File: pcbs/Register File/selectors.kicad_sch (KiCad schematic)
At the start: 1 part, among them U1001 74HC138

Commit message: More work
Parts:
- added R401 (x8): 220k, Resistor_SMD:R_0603_1608Metric, symbol Device:R
- added U1002, U1003, U1004: 74HC138, Package_DIP:DIP-16_W7.62mm_Socket, symbol 74xx:74HC138
- added U1005: 74HC540, Package_DIP:DIP-20_W7.62mm_Socket, symbol 74xx:74LS540
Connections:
- net +5V: now also U1002.16 (VCC), U1003.16 (VCC), U1004.16 (VCC), U1005.20 (VCC)
- net GND: now also R401.2, R401.2, R401.2, R401.2, R401.2, R401.2, R401.2, R401.2, U1002.8 (GND), U1003.8 (GND), U1004.8 (GND), U1005.10 (GND)
- new net: U1004.15 (~{Y0}), U1005.2 (A0)
- new net: U1004.14 (~{Y1}), U1005.3 (A1)
- new net: U1004.13 (~{Y2}), U1005.4 (A2)
- new net: U1004.12 (~{Y3}), U1005.5 (A3)
- new net: U1004.11 (~{Y4}), U1005.6 (A4)
- new net: U1004.10 (~{Y5}), U1005.7 (A5)
- new net: U1004.9 (~{Y6}), U1005.8 (A6)
- new net: U1004.7 (~{Y7}), U1005.9 (A7)
- new net C_{Write}0: R401.1, U1005.18 (Y0)
- new net C_{Write}1: R401.1, U1005.17 (Y1)
- new net C_{Write}2: R401.1, U1005.16 (Y2)
- new net C_{Write}3: R401.1, U1005.15 (Y3)
- new net C_{Write}4: R401.1, U1005.14 (Y4)
- new net C_{Write}5: R401.1, U1005.13 (Y5)
- new net C_{Write}6: R401.1, U1005.12 (Y6)
- new net C_{Write}7: R401.1, U1005.11 (Y7)
- new net R_{B}0: U1002.1 (A0)
- new net R_{B}1: U1002.2 (A1)
- new net R_{B}2: U1002.3 (A2)
- new net R_{C}0: U1003.1 (A0), U1004.1 (A0)
- new net R_{C}1: U1003.2 (A1), U1004.2 (A1)
- new net R_{C}2: U1003.3 (A2), U1004.3 (A2)
- new net ~{B_{select}}0: U1002.15 (~{Y0})
- new net ~{B_{select}}1: U1002.14 (~{Y1})
- new net ~{B_{select}}2: U1002.13 (~{Y2})
- new net ~{B_{select}}3: U1002.12 (~{Y3})
- new net ~{B_{select}}4: U1002.11 (~{Y4})
- new net ~{B_{select}}5: U1002.10 (~{Y5})
- new net ~{B_{select}}6: U1002.9 (~{Y6})
- new net ~{B_{select}}7: U1002.7 (~{Y7})
- new net ~{C_{select}}0: U1003.15 (~{Y0})
- new net ~{C_{select}}1: U1003.14 (~{Y1})
- new net ~{C_{select}}2: U1003.13 (~{Y2})
- new net ~{C_{select}}3: U1003.12 (~{Y3})
- new net ~{C_{select}}4: U1003.11 (~{Y4})
- new net ~{C_{select}}5: U1003.10 (~{Y5})
- new net ~{C_{select}}6: U1003.9 (~{Y6})
- new net ~{C_{select}}7: U1003.7 (~{Y7})
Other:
- moved on the sheet: U1001

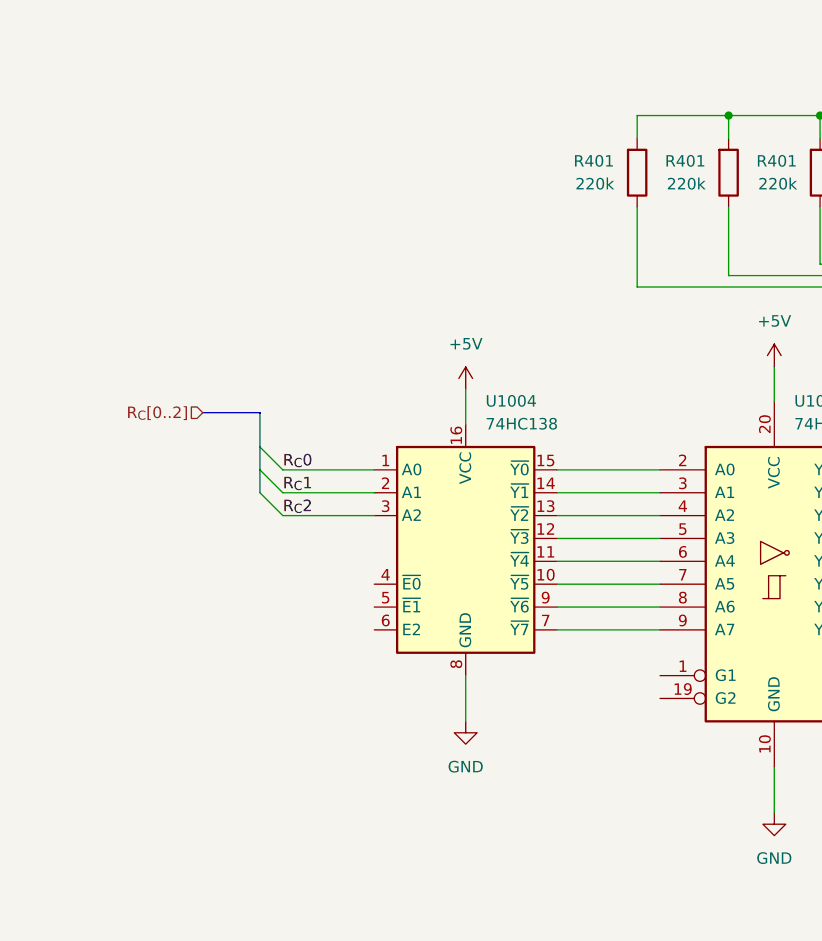
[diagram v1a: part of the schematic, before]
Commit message: Adding some capacitors
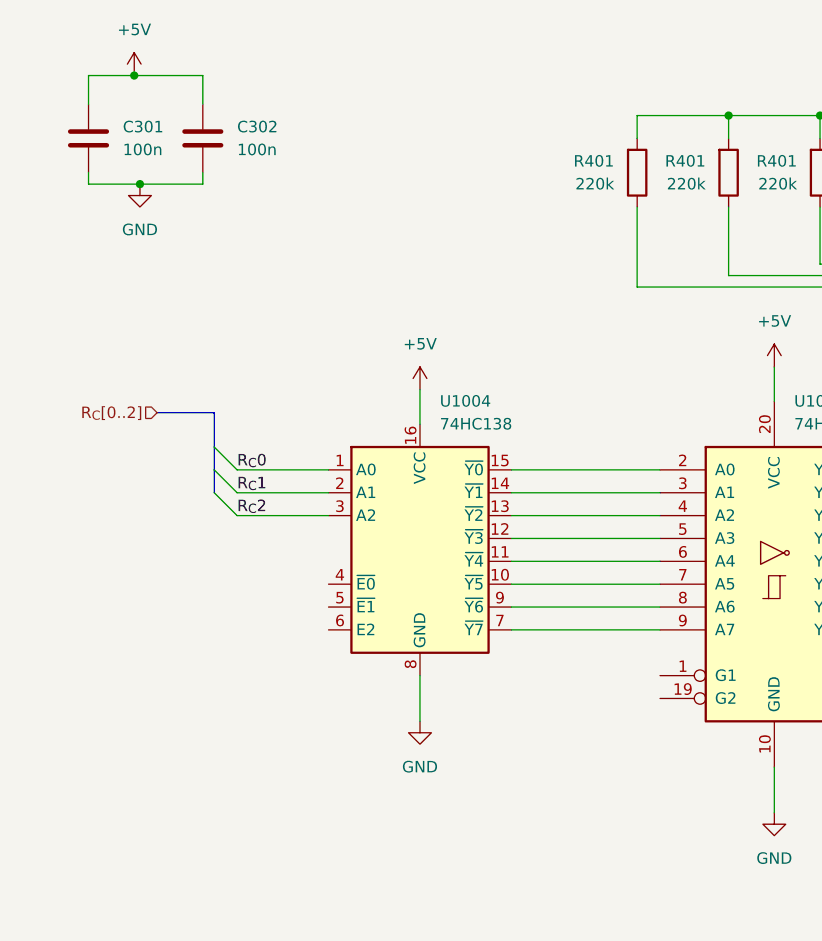
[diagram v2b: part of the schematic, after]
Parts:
- added C301, C302: 100n, Capacitor_SMD:C_0603_1608Metric, symbol Device:C
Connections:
- net +5V: now also C301.1, C302.1
- net GND: now also C301.2, C302.2
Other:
- moved on the sheet: U1004

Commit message: Lots of LEDs
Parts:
- added D801 (x8): YELLOW, LED_SMD:LED_0603_1608Metric, symbol Device:LED
- added R809, R810, R811, R812, R813, R814, R815, R816: 4k7, Resistor_SMD:R_0603_1608Metric, symbol Device:R
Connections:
- net +5V: now also D801.2 (A), D801.2 (A), D801.2 (A), D801.2 (A), D801.2 (A), D801.2 (A), D801.2 (A), D801.2 (A)
- net W0: now reaches U1004.15 (~{Y0}), U1005.2 (A0)
- net W0: now also R809.1
- net W1: now reaches U1004.14 (~{Y1}), U1005.3 (A1)
- net W1: now also R810.1
- net W2: now reaches U1004.13 (~{Y2}), U1005.4 (A2)
- net W2: now also R811.1
- net W3: now reaches U1004.12 (~{Y3}), U1005.5 (A3)
- net W3: now also R812.1
- net W4: now reaches U1004.11 (~{Y4}), U1005.6 (A4)
- net W4: now also R813.1
- net W5: now reaches U1004.10 (~{Y5}), U1005.7 (A5)
- net W5: now also R814.1
- net W6: now reaches U1004.9 (~{Y6}), U1005.8 (A6)
- net W6: now also R815.1
- net W7: now reaches U1004.7 (~{Y7}), U1005.9 (A7)
- net W7: now also R816.1
- new net: D801.1 (K), R815.2
- new net: D801.1 (K), R809.2
- new net: D801.1 (K), R811.2
- new net: D801.1 (K), R816.2
- new net: D801.1 (K), R814.2
- new net: D801.1 (K), R810.2
- new net: D801.1 (K), R813.2
- new net: D801.1 (K), R812.2

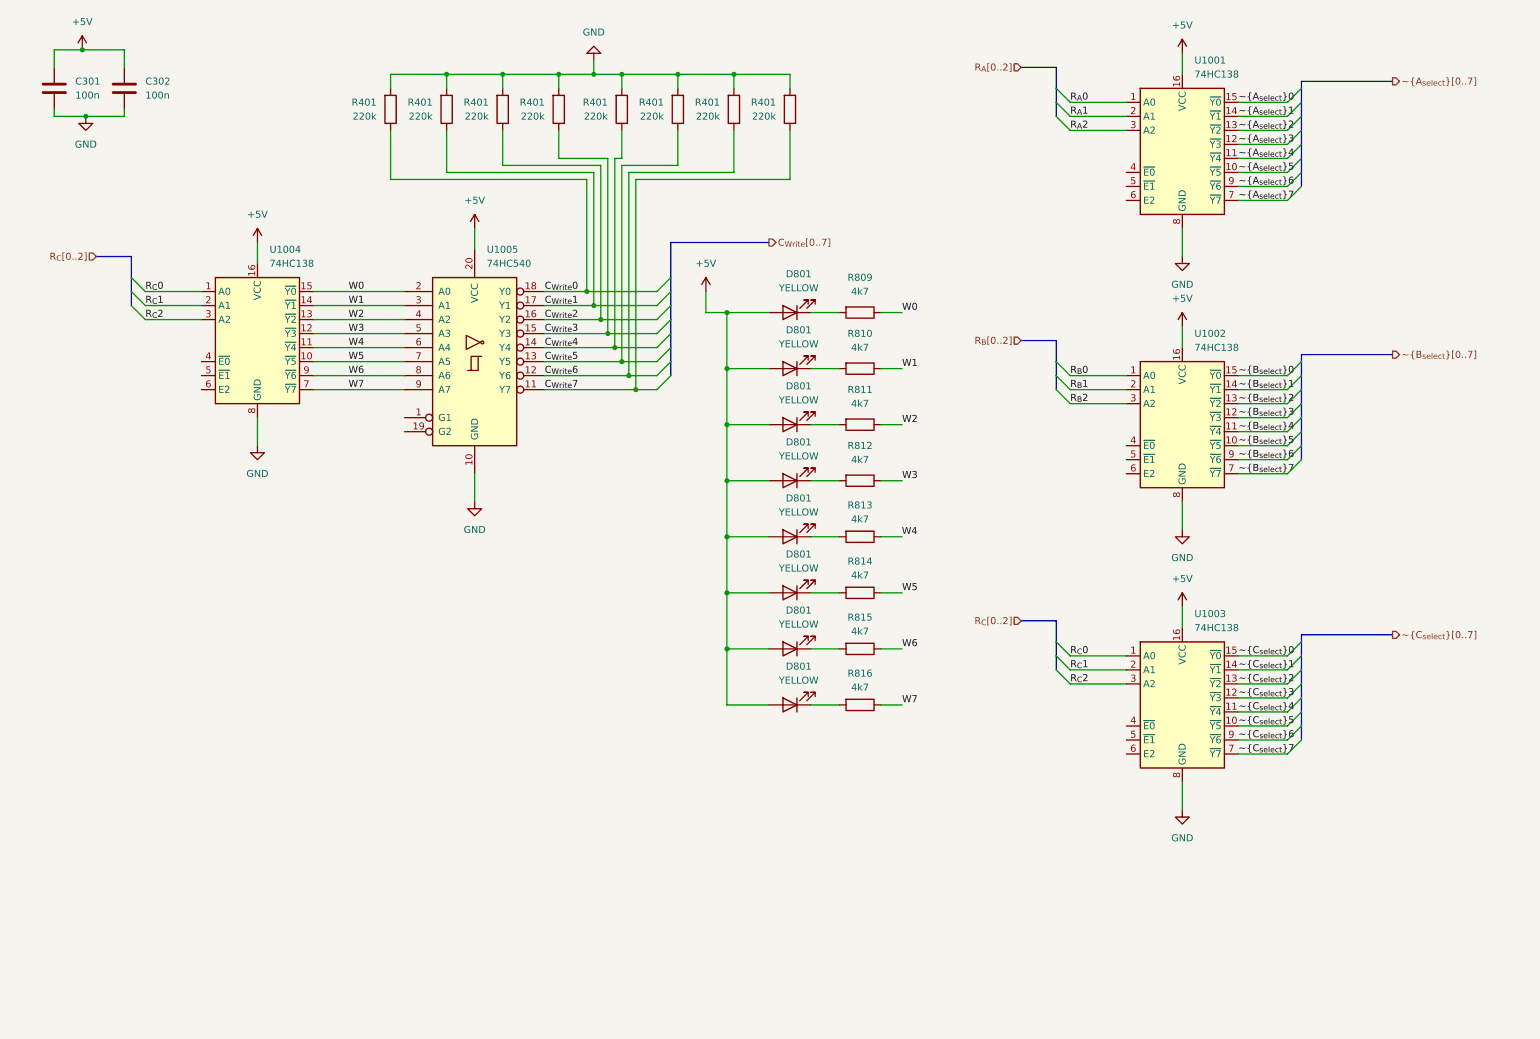
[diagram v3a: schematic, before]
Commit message: More control logic
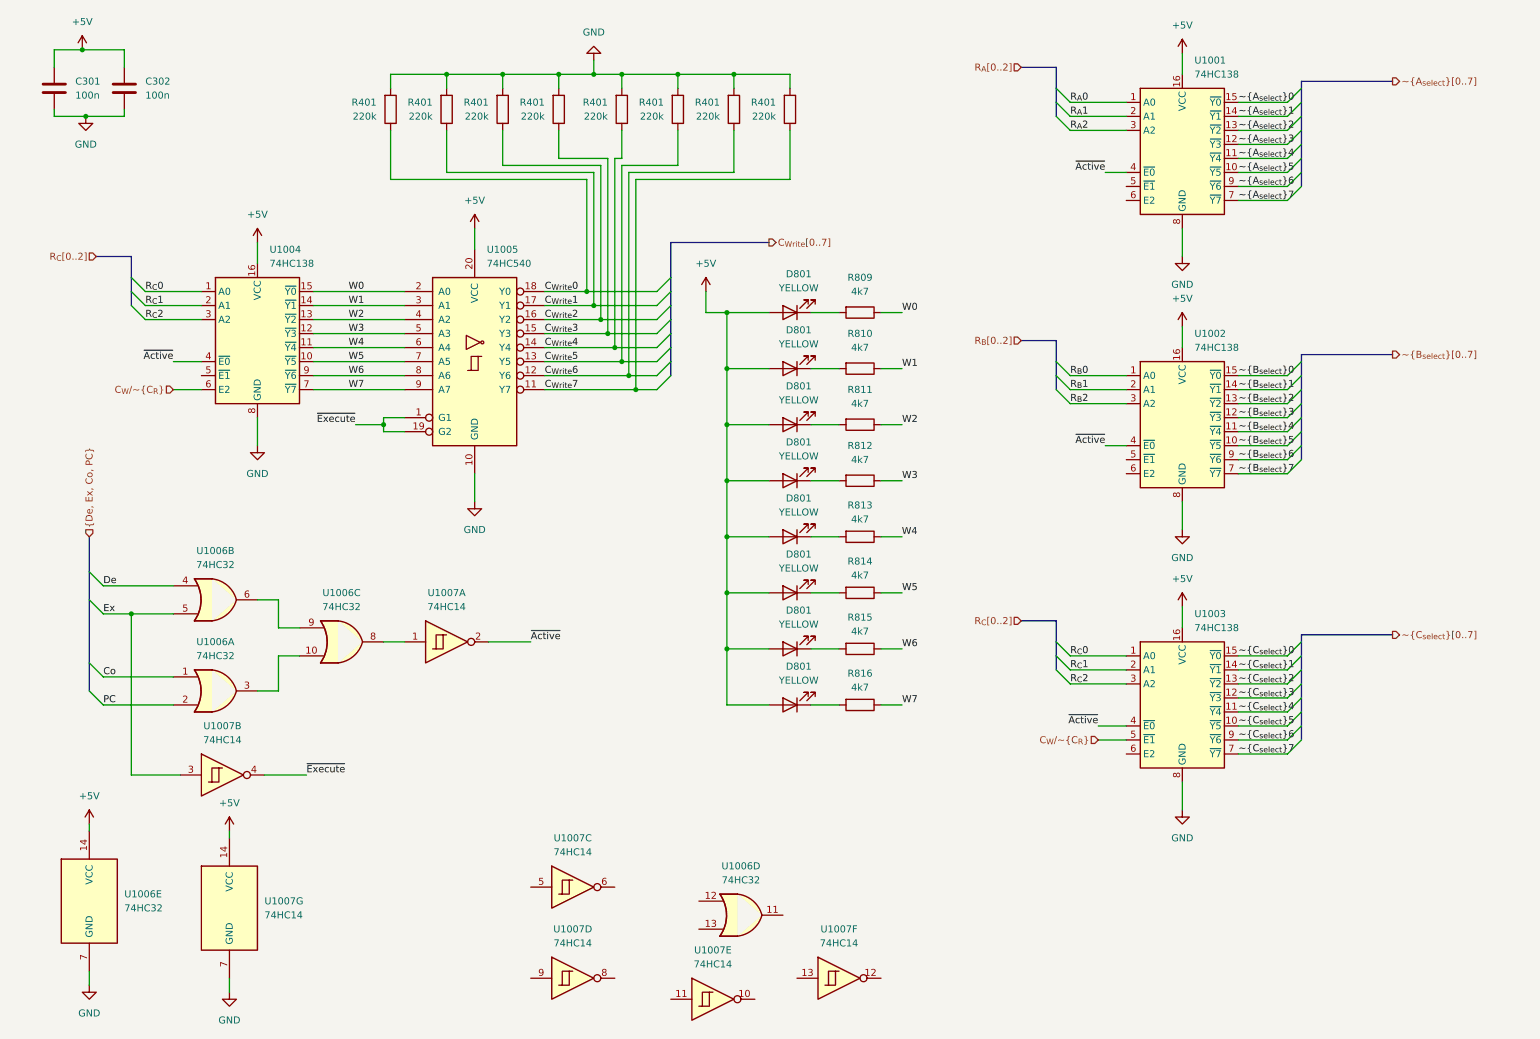
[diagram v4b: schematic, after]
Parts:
- added U1006: 74HC32, Package_DIP:DIP-14_W7.62mm_Socket, symbol 74xx:74LS32
- added U1007: 74HC14, Package_SO:SOIC-14_3.9x8.7mm_P1.27mm, symbol 74xx:74HC14
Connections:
- net +5V: now also U1006.14 (VCC), U1007.14 (VCC)
- net GND: now also U1006.7 (GND), U1007.7 (GND)
- net ~{Execute}: now reaches U1005.1 (G1)
- net ~{Execute}: now also U1005.19 (G2), U1007.4
- net ~{Active}: now reaches U1004.4 (~{E0})
- net ~{Active}: now also U1001.4 (~{E0}), U1002.4 (~{E0}), U1003.4 (~{E0}), U1007.2
- net C_{W}/~{C_{R}}: now reaches U1004.6 (E2)
- net C_{W}/~{C_{R}}: now also U1003.5 (~{E1})
- new net: U1006.6, U1006.9
- new net: U1006.10, U1006.3
- new net: U1006.8, U1007.1
- new net Co: U1006.1
- new net De: U1006.4
- new net Ex: U1006.5, U1007.3
- new net PC: U1006.2

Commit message: Routing the connector Pt 1 of n
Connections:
- net GND: now also U1006.12, U1006.13, U1007.11, U1007.13, U1007.5, U1007.9
- no-connect marks 0 -> 5

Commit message: Finish first draft routing. Need to silk screen
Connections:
- net +5V: now also U1001.6 (E2), U1002.6 (E2), U1003.6 (E2)
- net Co: now also U1006.12; no longer U1006.1
- net De: now also U1006.9; no longer U1006.4
- net Ex: now also U1006.10, U1007.11; no longer U1006.5, U1007.3
- net GND: now also U1001.5 (~{E1}), U1002.5 (~{E1}), U1004.5 (~{E1}), U1006.1, U1006.2, U1007.1, U1007.3; no longer U1006.12, U1006.13, U1007.11, U1007.13
- net PC: now also U1006.13; no longer U1006.2
- net ~{Active}: now also U1007.12; no longer U1007.2
- net ~{Execute}: now also U1007.10; no longer U1007.4
- net at U1006.11: now also U1006.4
- net at U1006.6: now also U1007.13; no longer U1006.9
- net at U1006.3: no longer U1006.10
- net at U1006.8: now also U1006.5; no longer U1007.1
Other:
- moved on the sheet: U1006A, U1006B, U1006C, U1006D, U1007A, U1007B, U1007E, U1007F
